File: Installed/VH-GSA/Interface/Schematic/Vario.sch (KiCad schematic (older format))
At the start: 2 parts

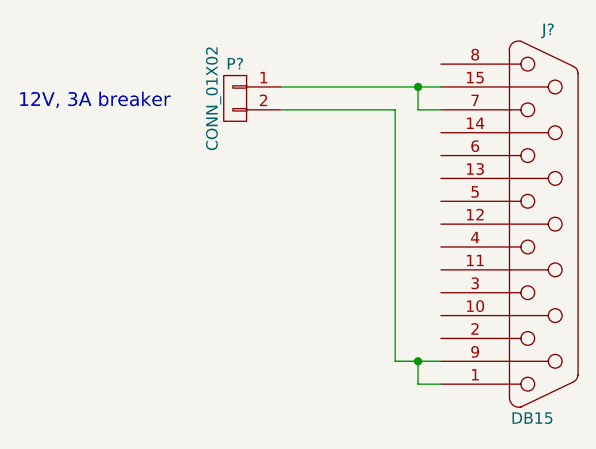
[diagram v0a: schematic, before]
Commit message: VH-GSA: Added OAT
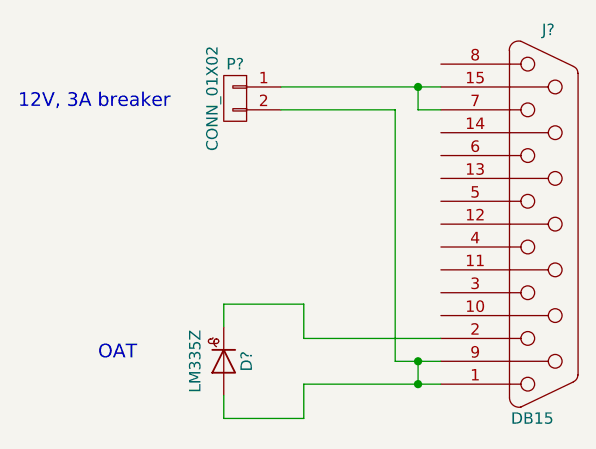
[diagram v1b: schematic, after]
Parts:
- added D?: LM335Z, symbol D_Temperature_Dependent
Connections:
- net at J?.1, J?.9 (P9), P?.2 (P2): now also D?.2 (A)
- net at J?.2: now also D?.1 (K)
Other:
- note added: "OAT"
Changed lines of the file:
@@
 	2900 4500 2900 4600
 Wire Wire Line
-	2900 4600 3000 4600
+	2400 4600 3000 4600
 $Comp
 L CONN_01X02 P?
@@
 Text Notes 1150 3400 0    60   ~ 0
 12V, 3A breaker
+$Comp
+L D_Temperature_Dependent D?
+U 1 1 5DCABD0C
+P 2050 4500
+F 0 "D?" H 2050 4600 50  0000 C CNN
+F 1 "LM335Z" H 2050 4375 50  0000 C CNN
+F 2 "" H 2050 4500 50  0000 C CNN
+F 3 "" H 2050 4500 50  0000 C CNN
+	1    2050 4500
+	0    1    1    0
+$EndComp
+Wire Wire Line
+	2400 4600 2400 4750
+Wire Wire Line
+	2400 4750 2050 4750
+Wire Wire Line
+	2050 4750 2050 4650
+Connection ~ 2900 4600
+Wire Wire Line
+	3000 4400 2400 4400
+Wire Wire Line
+	2400 4400 2400 4250
+Wire Wire Line
+	2400 4250 2050 4250
+Wire Wire Line
+	2050 4250 2050 4350
+Text Notes 1500 4500 0    60   ~ 0
+OAT
 $EndSCHEMATC
